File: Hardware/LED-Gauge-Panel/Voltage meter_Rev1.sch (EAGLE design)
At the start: 31 parts, among them J3 SL04, Q4 MOSFET-NCHANNEL2N7002PW, Q5 MOSFET-NCHANNEL2N7002PW, Q6 MOSFET-NCHANNEL2N7002PW, U1 ATMEGA328P_PDIP, U21 MAX232D, X1 22-23-2031, X2 16MHz

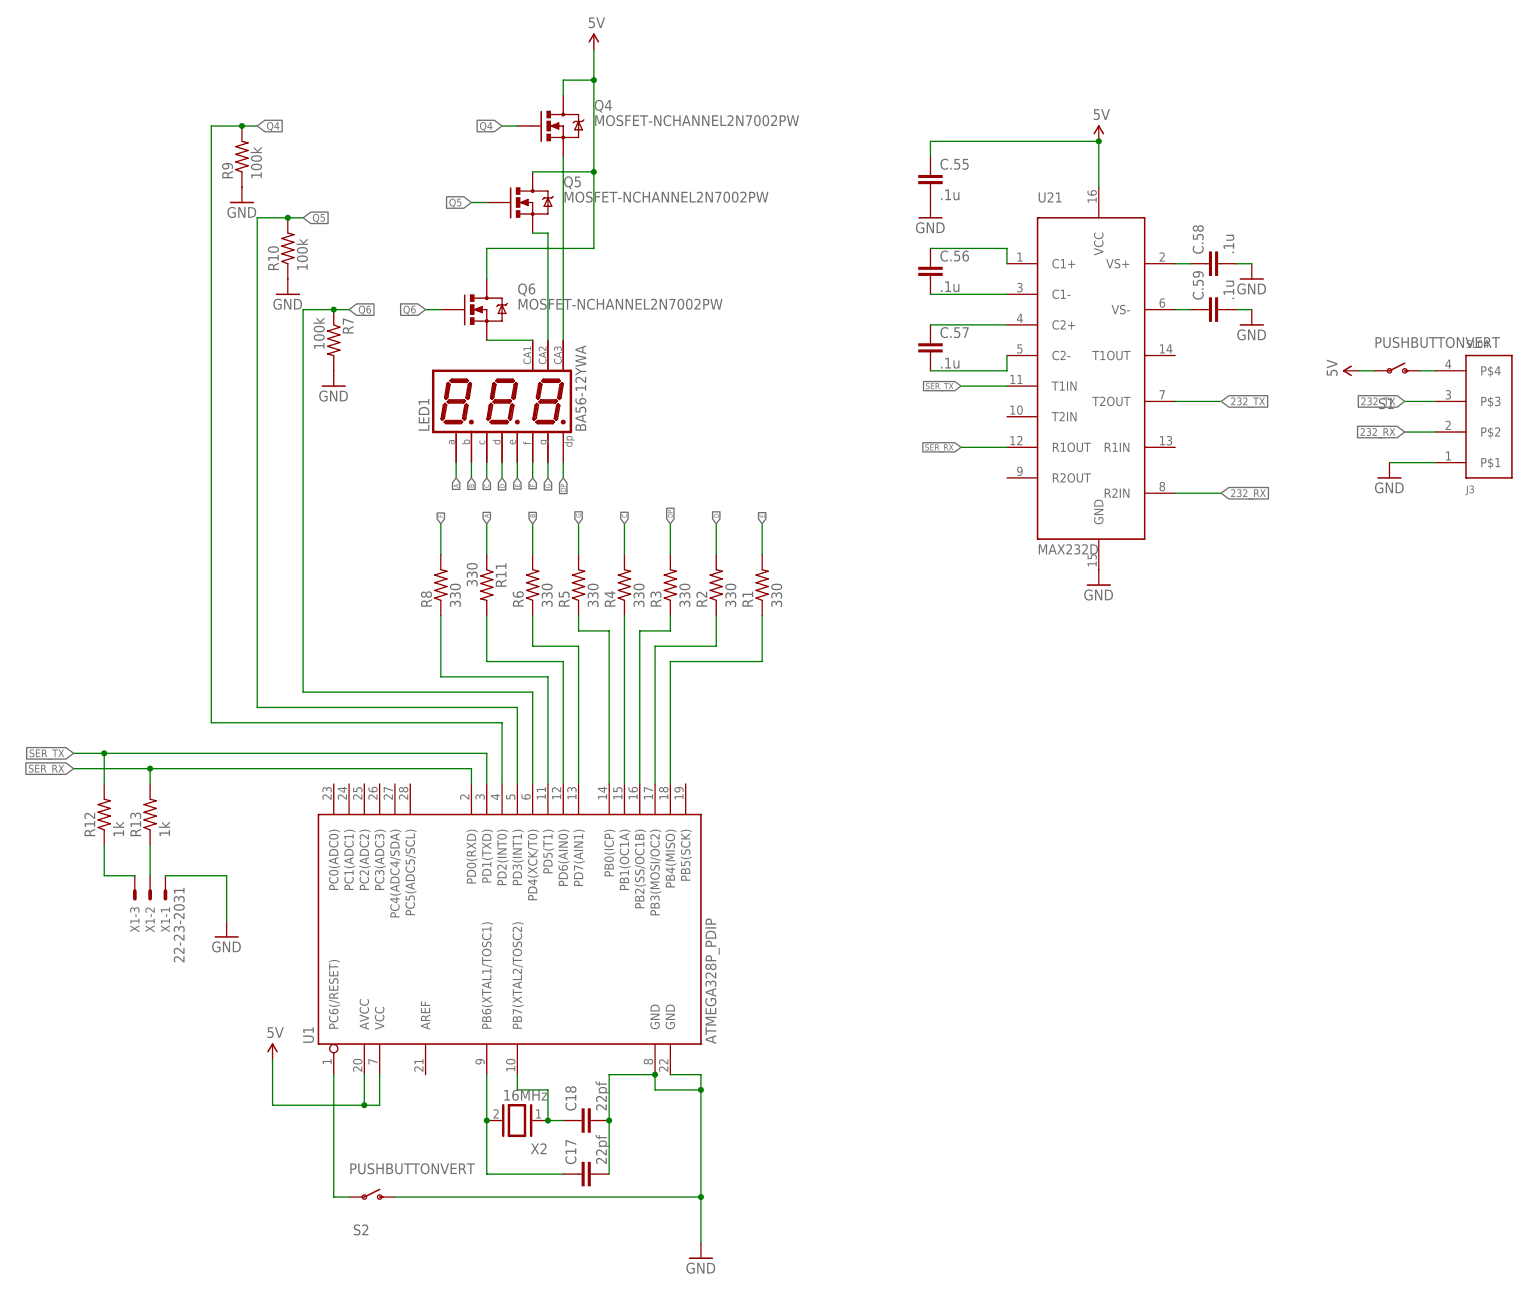
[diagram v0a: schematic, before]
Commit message: Review 2 changes
Changed from n channel mosfets to p channel. Removed the resistors on
the control lines to the mosfets.
moved the resistors in series with the programming pins. And put
capacitors in the VCC lines.
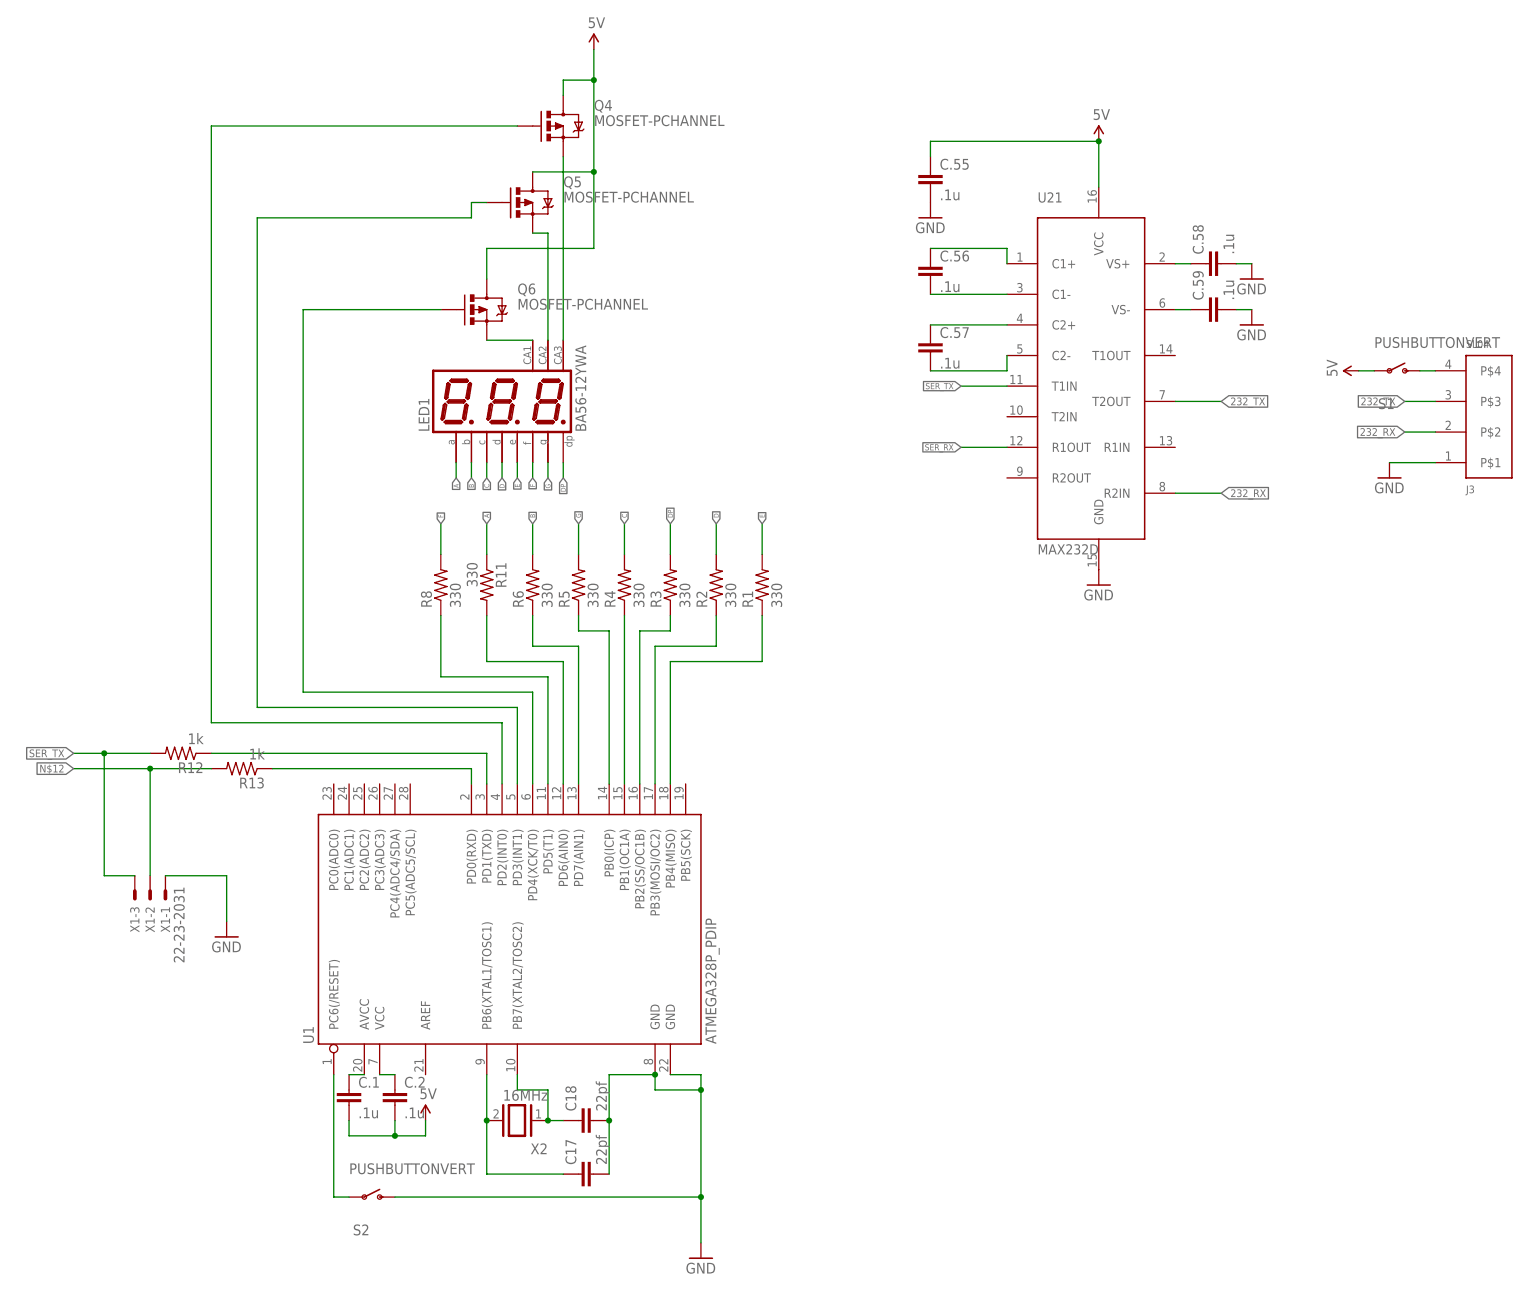
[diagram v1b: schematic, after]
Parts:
- removed R10, R7, R9: 100k, SparkFun-Passives:RESISTOR0805-RES
- added C.1, C.2: .1u, SparkFun-Passives:CAP0805
- Q4, Q5, Q6: value MOSFET-NCHANNEL2N7002PW -> MOSFET-PCHANNEL; device SparkFun-DiscreteSemi:MOSFET-NCHANNEL2N7002PW -> SparkFun-DiscreteSemi:MOSFET-PCHANNEL
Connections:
- new net N$15: C.2.1, U1.VCC
- new net N$16: C.1.1, U1.AVCC
- net 5V: now also C.1.2, C.2.2; no longer U1.AVCC, U1.VCC
- net GND: no longer R10.1, R7.2, R9.1
- net N$12: now also R13.2; no longer R13.1
- net N$14: now also R12.2; no longer R12.1
- net Q4: no longer R9.2
- net Q5: no longer R10.2
- net Q6: no longer R7.1
- net SER_RX: now also R13.1; no longer R13.2
- net SER_TX: now also R12.1; no longer R12.2
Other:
- moved on the sheet: R12, R13

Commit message: Modifications from second review
The atmega chip was changed to be surface mount. Wires were rerouted and
DRC was run. Capacitors added as well.
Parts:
- U1: value ATMEGA328P_PDIP -> ATMEGA328P_PDIPDIL28-4; device SparkFun-DigitalIC:ATMEGA328P_PDIP -> SparkFun-DigitalIC:ATMEGA328P_PDIPDIL28-4
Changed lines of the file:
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@@
 <part name="SUPPLY4" library="SparkFun-Aesthetics" deviceset="5V" device=""/>
 <part name="SUPPLY5" library="SparkFun-Aesthetics" deviceset="5V" device=""/>
-<part name="U1" library="SparkFun-DigitalIC" deviceset="ATMEGA328P_PDIP" device=""/>
+<part name="U1" library="SparkFun-DigitalIC" deviceset="ATMEGA328P_PDIP" device="DIL28-4" value="ATMEGA328P_PDIPDIL28-4"/>
 <part name="S2" library="MRDT-UserInput" deviceset="PUSHBUTTON" device="VERT"/>
 <part name="SUPPLY1" library="SparkFun-Aesthetics" deviceset="5V" device=""/>

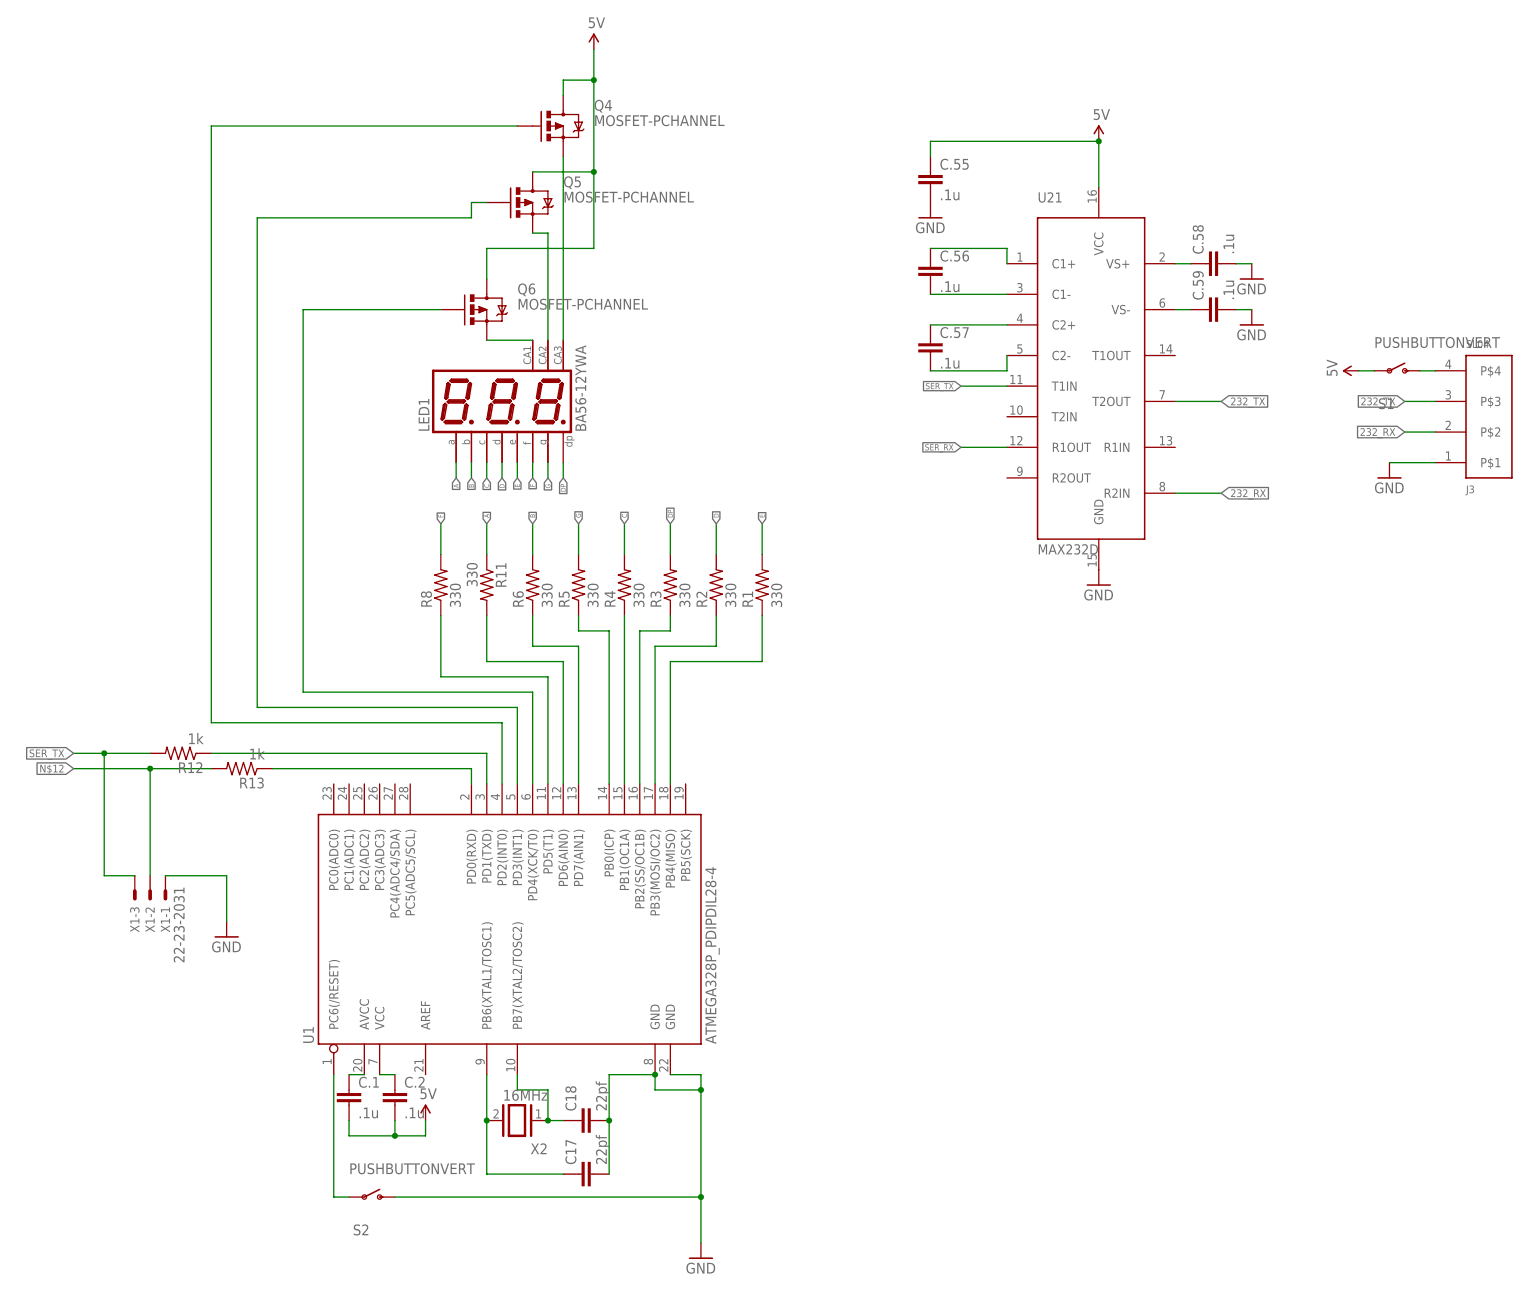
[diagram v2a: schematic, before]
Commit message: Reroute and label
Minor changes made to the positioning of the capacitors. Some traces
were changed due to the capacitor changes and some changes were made to
keep the trace from jumping between levels. Labels were positioned on
the board and MRDT symbol was placed on the board as well as a brief
board discription.
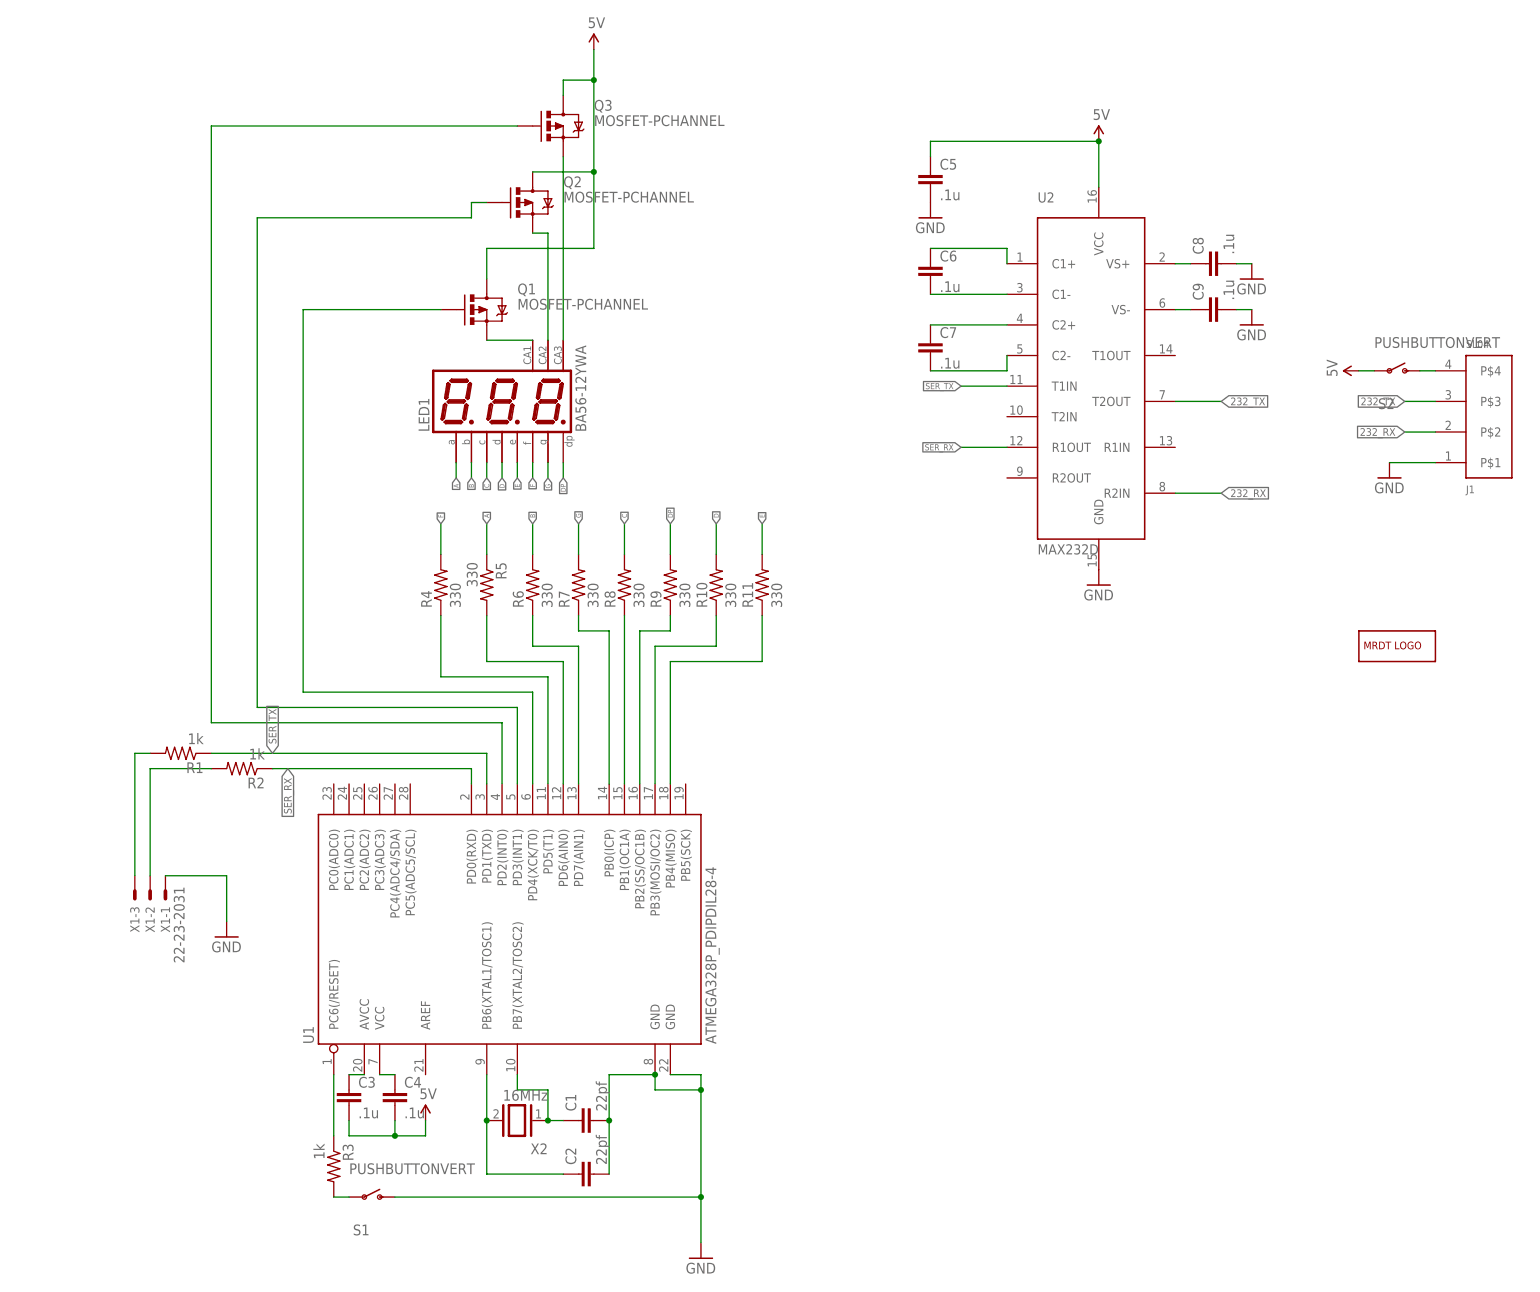
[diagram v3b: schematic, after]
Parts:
- removed R12, R13: 1k, SparkFun-Passives:RESISTOR0805-RES
- added LOGO1: MRDT_LOGO, MRDT-Hardware:MRDT_LOGO
- added R10, R7, R9: 330, SparkFun-Passives:RESISTOR0805-RES
- R1, R2, R3: value 330 -> 1k
- renumbered C.1 to C3, C.2 to C4, C.55 to C5, C.56 to C6, C.57 to C7, C.58 to C8, C.59 to C9, C17 to C2, C18 to C1, J3 to J1, Q4 to Q3, Q5 to Q2, Q6 to Q1, U21 to U2
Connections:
- new net N$24: R3.1, U1.PC6(/RESET)
- net 5V: now also S2.P; no longer S1.P
- net A: now also R5.1; no longer R11.1
- net C: now also R8.2; no longer R4.2
- net D: now also R10.2; no longer R2.2
- net DP: now also R9.2; no longer R3.2
- net E: now also R11.2; no longer R1.2
- net F: now also R4.2; no longer R8.2
- net G: now also R7.2; no longer R5.2
- net GND: now also S1.S; no longer S2.S
- net N$1: now also R7.1; no longer R5.1
- net N$10: now also R11.1; no longer R1.1
- net N$12: now also R2.2; no longer R13.2
- net N$13: now also R3.2, S1.P; no longer S2.P, U1.PC6(/RESET)
- net N$14: now also R1.2; no longer R12.2
- net N$20: now also R4.1; no longer R8.1
- net N$5: now also R8.1; no longer R4.1
- net N$6: now also R9.1; no longer R3.1
- net N$7: now also S2.S; no longer S1.S
- net N$8: now also R5.2; no longer R11.2
- net N$9: now also R10.1; no longer R2.1
- net SER_RX: now also R2.1; no longer R13.1
- net SER_TX: now also R1.1; no longer R12.1
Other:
- moved on the sheet: R1, R11, R2, R3, R4, R5, R8, S1, S2
